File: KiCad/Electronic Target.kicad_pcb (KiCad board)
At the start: 2 copper layers, 41 parts, among them J1 BERG 5x2, J2 Conn_02x04_Odd_Even, U1 LM339, U2 74HC74, U3 74HC74, U4 74HC00, U5 74LV8154, U6 74LV8154, X1 8M0

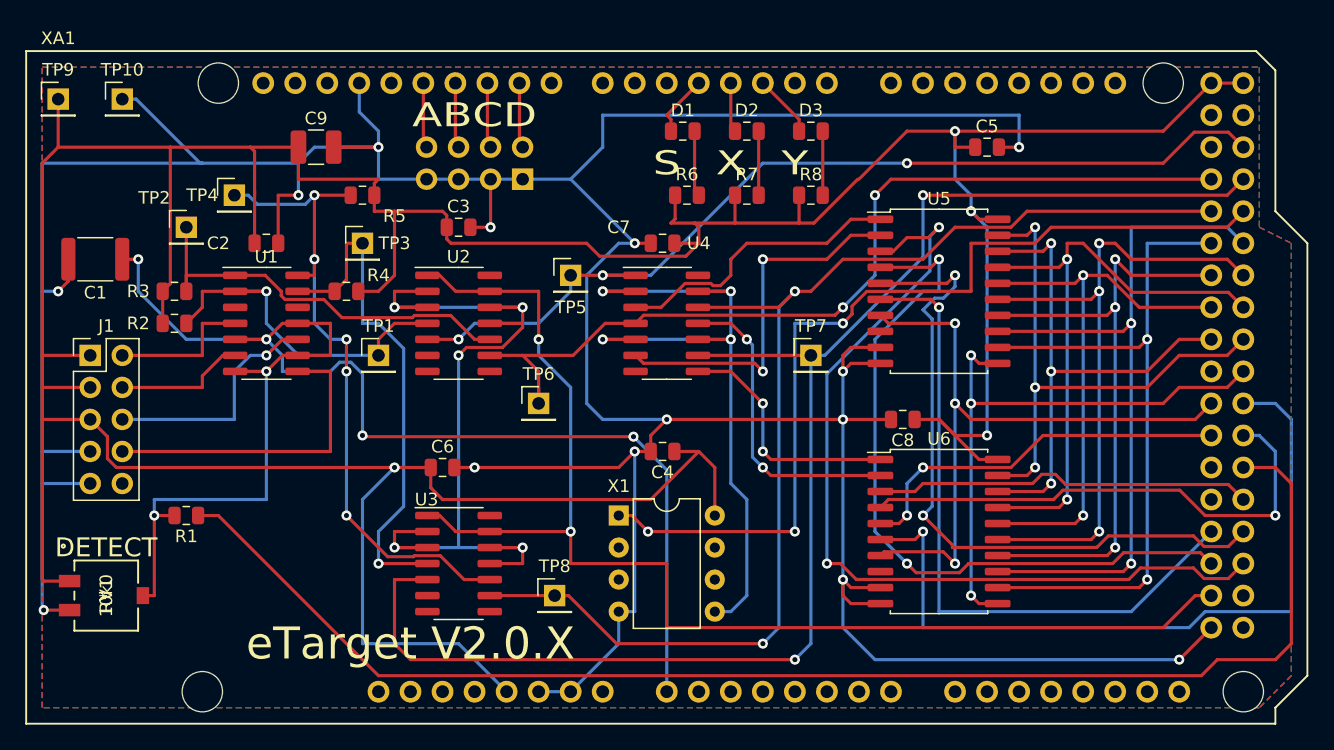
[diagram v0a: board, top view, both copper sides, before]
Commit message: Cleaning up documentation
Sorry, but the folders were a bit disorganized,

Cleaned up the folders and added a PDF of the schematic
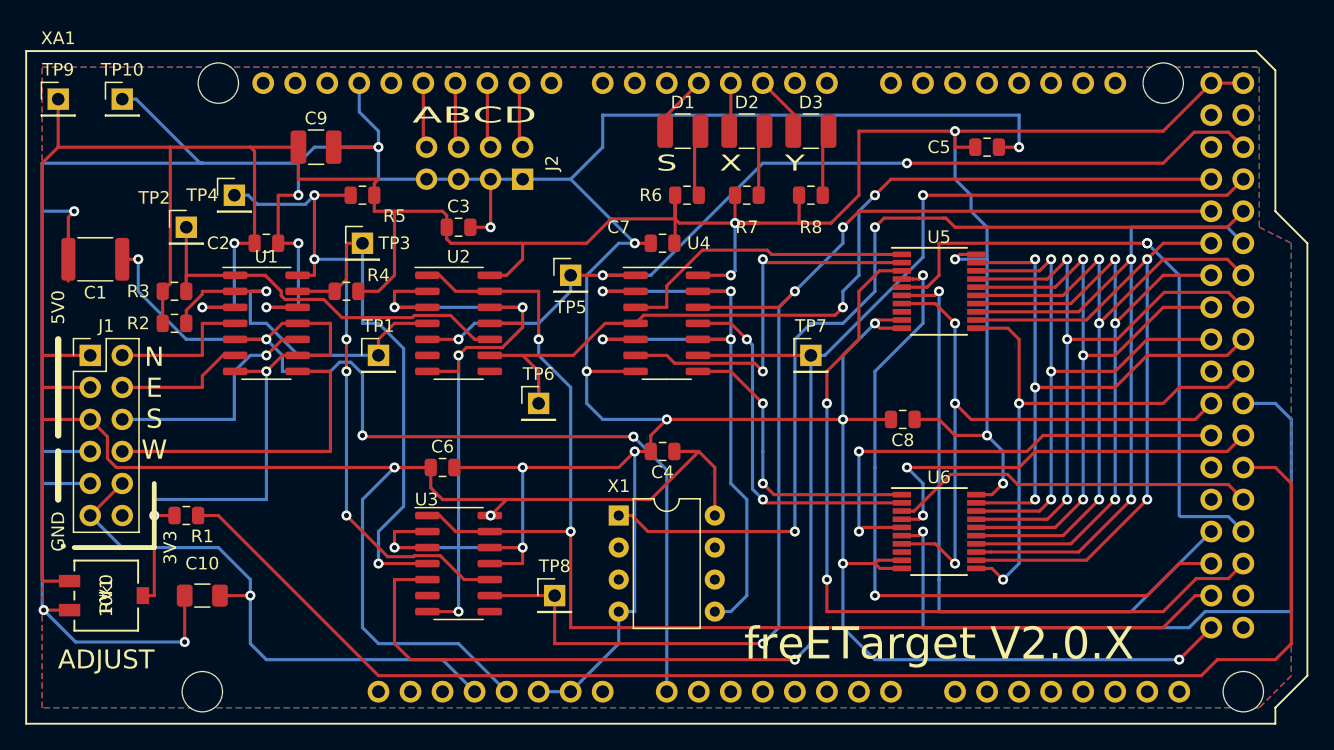
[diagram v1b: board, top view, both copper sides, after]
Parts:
- added C10: 10uF0, Resistor_SMD:R_1206_3216Metric, F.Cu at (130.8, 125.7)
- D1, D2, D3: footprint Resistor_SMD:R_0805_2012Metric -> Resistor_SMD:R_1210_3225Metric
- J1: value BERG 5x2 -> BERG 2x6; footprint Connector_PinHeader_2.54mm:PinHeader_2x05_P2.54mm_Vertical -> Connector_PinHeader_2.54mm:PinHeader_2x06_P2.54mm_Vertical
- U5, U6: footprint Package_SO:SOIC-20W_7.5x12.8mm_P1.27mm -> Package_SO:TSSOP-20_4.4x6.5mm_P0.65mm
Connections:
- J1 pad 10: (no net) -> Net-(C10-Pad1)
- U1 pad 12: (no net) -> GND
- U1 pad 3: (no net) -> VCC
- U2 pad 11: Net-(U2-Pad11) -> GND
- U2 pad 12: Net-(U2-Pad11) -> GND
- U2 pad 14: (no net) -> VCC
- U2 pad 2: Net-(U2-Pad11) -> GND
- U2 pad 3: Net-(U2-Pad11) -> GND
- U2 pad 7: (no net) -> GND
- U3 pad 11: Net-(U2-Pad11) -> GND
- U3 pad 12: Net-(U2-Pad11) -> GND
- U3 pad 14: (no net) -> VCC
- U3 pad 2: Net-(U2-Pad11) -> GND
- U3 pad 3: Net-(U2-Pad11) -> GND
- U3 pad 7: (no net) -> GND
- U4 pad 14: (no net) -> VCC
- U4 pad 7: (no net) -> GND
- XA1 pad 3V3: Net-(XA1-Pad3V3) -> Net-(C10-Pad1)
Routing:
- net GND: track 327.5 -> 449.5 mm, vias 14 -> 24
- net Net-(U2-Pad11): track 67.8 -> 0.00 mm, vias 5 -> 0
- net Net-(C10-Pad1): track 0.00 -> 45.2 mm, vias 0 -> 1
- net VCC: track 336.1 -> 365.6 mm, vias 4 -> 10
- net /WEST_LO*: track 30.6 -> 38.4 mm
- net /SOUTH_HI*: track 40.9 -> 33.9 mm, vias 1 -> 2
- net /NORTH_LO*: track 70.6 -> 65.1 mm
- net /D3: track 44.3 -> 49.6 mm, vias 2 -> 3
- net /EAST_LO*: track 55.1 -> 50.6 mm
- net Net-(U4-Pad8): track 19.6 -> 23.9 mm
- net Net-(U4-Pad11): track 24.7 -> 28.8 mm
- net /D5: track 50.2 -> 54.1 mm
- net /D1: track 41.8 -> 45.4 mm
- net /D0: track 43.6 -> 46.7 mm
- net /D4: track 52.0 -> 55.0 mm
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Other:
- board text added: "3V3"
- board text added: "5V0"
- board text added: "ADJUST"
- board text added: "GND"
- board text added: "N E S W"
- board text added: "freETarget V2.0.X"
- board text removed: "DETECT"
- board text removed: "eTarget V2.0.X"

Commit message: Adding Interface Control Document
This details the interface between the Arduino target aquisition board and the display PC
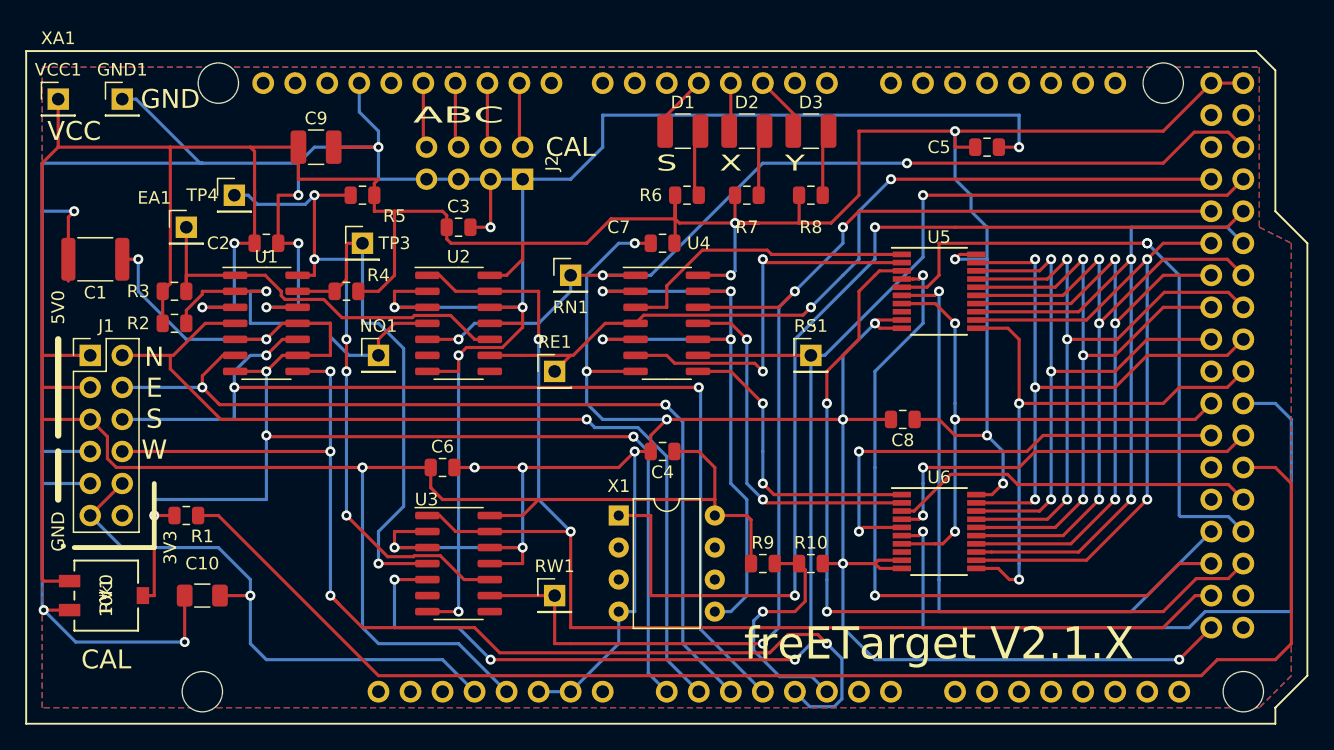
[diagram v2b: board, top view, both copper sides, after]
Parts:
- added R10: 4K7, Resistor_SMD:R_0805_2012Metric, F.Cu at (179.1, 123.2)
- added R9: 4K7, Resistor_SMD:R_0805_2012Metric, F.Cu at (175.3, 123.2)
- R1: value R -> 4K7
- TP3: value TP -> SO
- TP4: value TP -> WE
- moved RE1 2.84 mm to (158.8, 108.0)
- renumbered TP2 to EA1, TP10 to GND1, TP1 to NO1, TP6 to RE1, TP5 to RN1, TP7 to RS1, TP8 to RW1, TP9 to VCC1
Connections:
- XA1 pad A1: Net-(XA1-PadA1) -> /MIC_NORTH
- XA1 pad A2: Net-(XA1-PadA2) -> /MIC_EAST
- XA1 pad A3: Net-(XA1-PadA3) -> /MIC_SOUTH
- XA1 pad A4: Net-(XA1-PadA4) -> /MIC_WEST
- XA1 pad A5: Net-(XA1-PadA5) -> /BD_REV
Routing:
- net /MIC_SOUTH: track 18.8 -> 84.2 mm, vias 1 -> 3
- net /MIC_WEST: track 25.5 -> 89.3 mm, vias 0 -> 4
- net /MIC_EAST: track 10.5 -> 72.7 mm, vias 0 -> 3
- net /MIC_NORTH: track 11.5 -> 73.0 mm, vias 0 -> 1
- net /BD_REV: track 0.00 -> 19.4 mm, vias 0 -> 1
- net /QUIET: track 73.1 -> 81.9 mm
- net VCC: track 365.6 -> 373.4 mm, vias 10 -> 9
- net /V_FB: track 121.4 -> 114.0 mm
- net /RUN_EAST: track 72.3 -> 67.0 mm
- net GND: track 449.5 -> 454.1 mm, vias 24 -> 25
- net /READ*: track 50.2 -> 46.8 mm
- net /SOUTH_HI*: track 33.9 -> 32.1 mm
- net /CLR*: track 44.7 -> 45.4 mm
- net /RUN_SOUTH: track 116.5 -> 115.8 mm, vias 2 -> 4
- net Net-(NO1-Pad1): track 29.2 -> 29.8 mm
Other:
- board text added: "ABC"
- board text added: "CAL"
- board text added: "VCC"
- board text added: "freETarget V2.1.X"
- board text removed: "ABCD"
- board text removed: "ADJUST"
- board text removed: "freETarget V2.0.X"

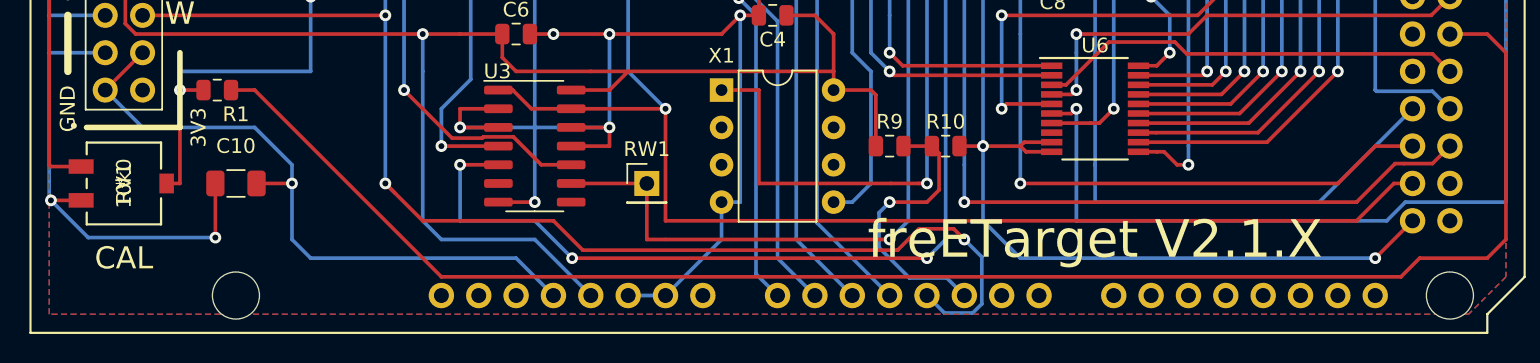
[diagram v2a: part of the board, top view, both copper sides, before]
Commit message: Sensor Module
This commit updates the sensor module  for experimental evaluation
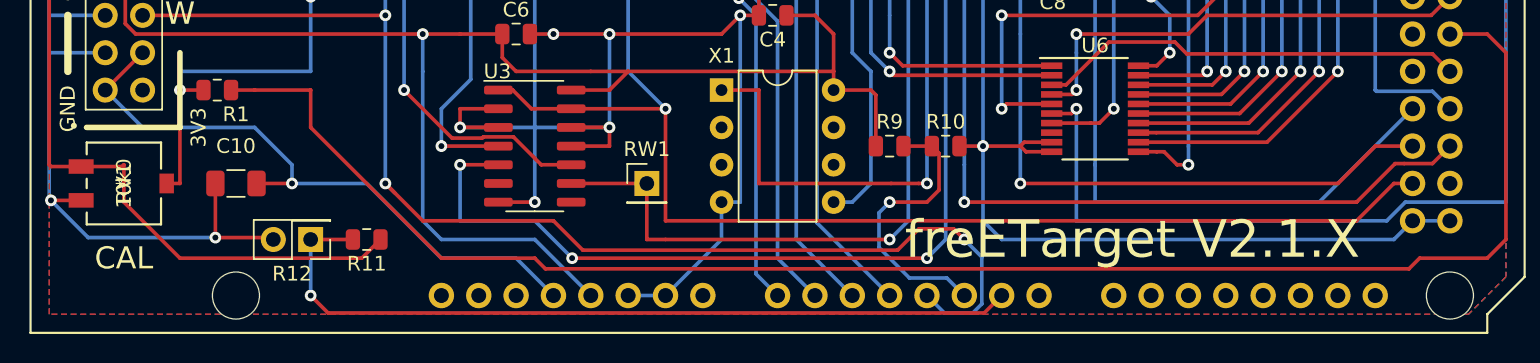
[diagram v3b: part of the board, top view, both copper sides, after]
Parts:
- added R11: 10k0, Resistor_SMD:R_0805_2012Metric, F.Cu at (139.7, 129.5)
- added R12: RTD, Connector_PinHeader_2.54mm:PinHeader_2x01_P2.54mm_Vertical, F.Cu at (135.9, 129.5)
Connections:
- XA1 pad A6: Net-(XA1-PadA6) -> /TEMP
- XA1 pad GND6: Net-(XA1-PadGND6) -> GND
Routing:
- net /TEMP: track 0.00 -> 54.7 mm, vias 0 -> 1
- net VCC: track 373.4 -> 398.4 mm
- net GND: track 454.1 -> 459.6 mm, vias 25 -> 24
- net Net-(C10-Pad1): track 45.2 -> 43.0 mm
- net /VREF: track 110.0 -> 111.1 mm

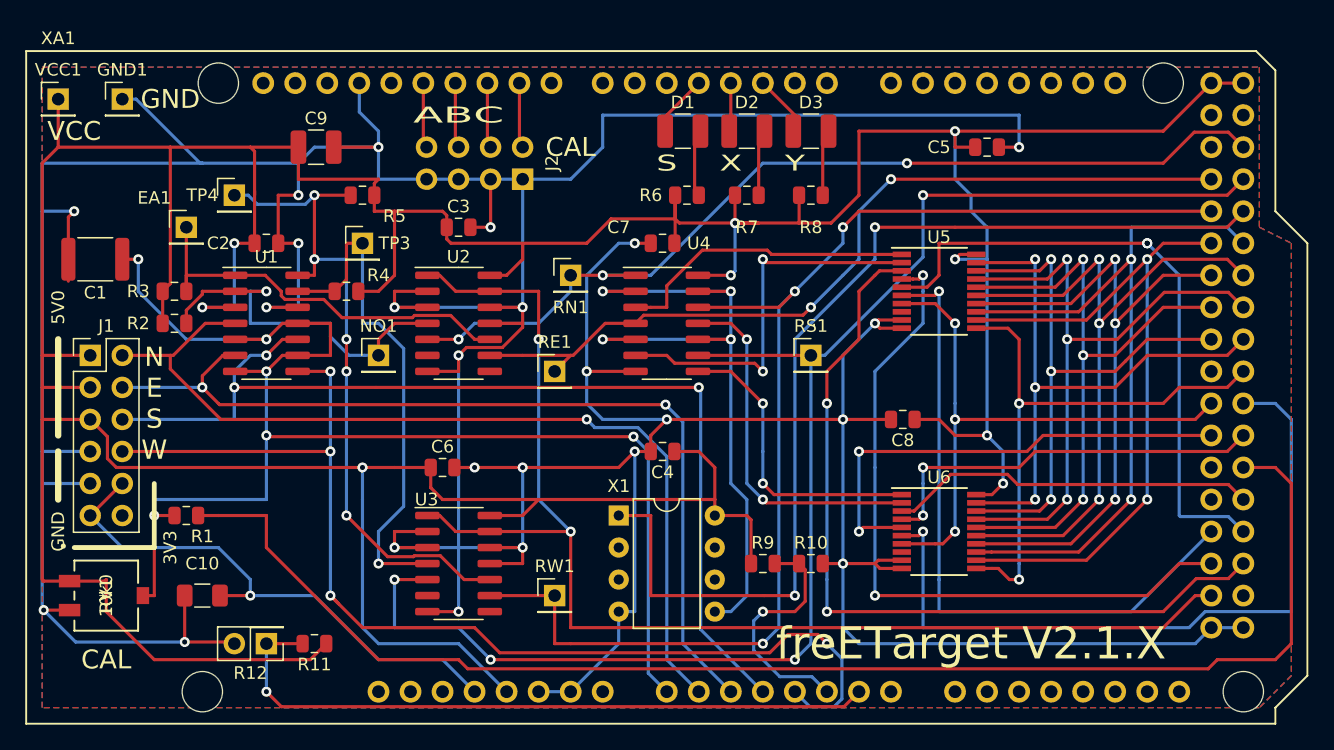
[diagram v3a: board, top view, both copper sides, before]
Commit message: Circuit Rev 2
Added negative power supply to drive sensor boards
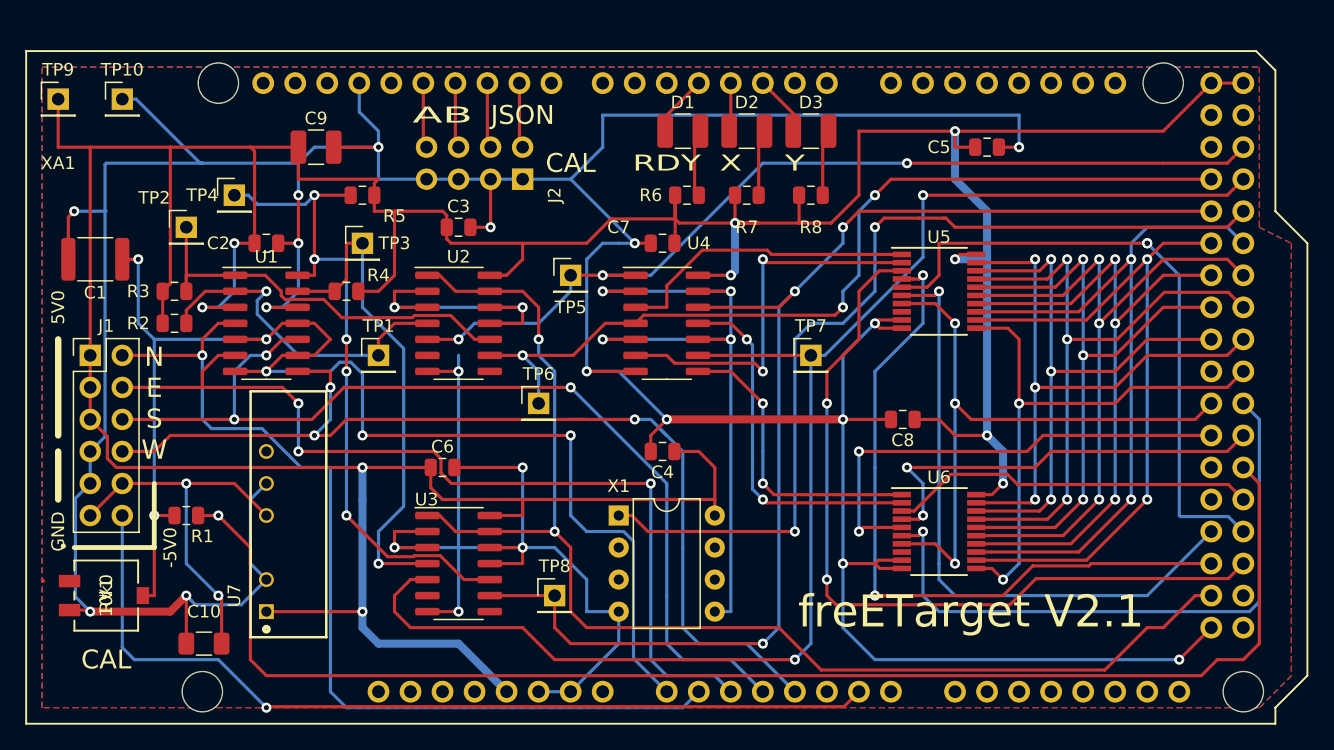
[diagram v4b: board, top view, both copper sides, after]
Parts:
- removed R10, R9: 4K7, Resistor_SMD:R_0805_2012Metric
- removed R11: 10k0, Resistor_SMD:R_0805_2012Metric
- removed R12: RTD, Connector_PinHeader_2.54mm:PinHeader_2x01_P2.54mm_Vertical
- added U7: NMA0505SC, NMA0505SC:SIP600W50P254L1950H1000Q5, F.Cu at (135.9, 127.0)
- J1: value BERG 2x6 -> Conn_02x06_Odd_Even
- TP3: value SO -> TP
- TP4: value WE -> TP
- moved C10 3.81 mm to (130.9, 129.5)
- moved TP6 2.84 mm to (157.5, 110.5)
- renumbered NO1 to TP1, GND1 to TP10, EA1 to TP2, RN1 to TP5, RE1 to TP6, RS1 to TP7, RW1 to TP8, VCC1 to TP9
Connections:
- J1 pad 12: (no net) -> /TEMP
- XA1 pad 3V3: Net-(C10-Pad1) -> Net-(XA1-Pad3V3)
- XA1 pad GND6: GND -> Net-(XA1-PadGND6)
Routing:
- net VCC: track 398.4 -> 346.5 mm, vias 9 -> 10
- net GND: track 459.6 -> 424.4 mm, vias 24 -> 23
- net /BD_REV: track 19.4 -> 0.00 mm, vias 1 -> 0
- net /TEMP: track 54.7 -> 71.3 mm
- net Net-(C10-Pad1): track 43.0 -> 29.9 mm, vias 1 -> 2
- net /QUIET: track 81.9 -> 73.1 mm
- net /WEST_HI*: track 58.7 -> 50.7 mm
- net /MIC_WEST: track 89.3 -> 81.9 mm, vias 4 -> 3
- net /MIC_SOUTH: track 84.2 -> 79.2 mm
- net /RUN_EAST: track 67.0 -> 71.1 mm, vias 2 -> 3
- net /READ*: track 46.8 -> 50.2 mm
- net Net-(R2-Pad2): track 29.8 -> 27.1 mm
- net /MIC_NORTH: track 73.0 -> 75.6 mm
- net /EAST_HI*: track 52.7 -> 50.2 mm
- net /V_FB: track 114.0 -> 112.1 mm
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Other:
- board text added: "-5V0"
- board text added: "AB"
- board text added: "JSON"
- board text added: "RDY"
- board text added: "freETarget V2.1"
- board text removed: "3V3"
- board text removed: "ABC"
- board text removed: "S"
- board text removed: "VCC"
- board text removed: "freETarget V2.1.X"
